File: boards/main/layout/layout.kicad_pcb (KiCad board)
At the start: 4 copper layers, 200 x 100 mm, 115 parts, among them J1 PPPC201LFBN-RC, J10 61300811121, J11 61300811121, J12 SJ1-3523N, J13 61300311121, J14 61300311121, J15 61300811121, J16 61300811121, J17 61300811121, J18 61300811121, J19 USB4085-GF-A, J2 PPPC201LFBN-RC, J3 61301021121, J4 connector, J5 61300211121, J6 61300211121, J7 SJ1-3523N, J8 61300811121, J9 61300811121, U1 ES8388, U10 NE5532DR, U2 ES8388, U3 LP2985-33DBVR, U4 MCP73831-2-OTI/OT, U5 HT8988A, U6 AP2114H-3.3TRG1, U7 CD4052BM96, U8 CD4052BM96, U9 NE5532DR

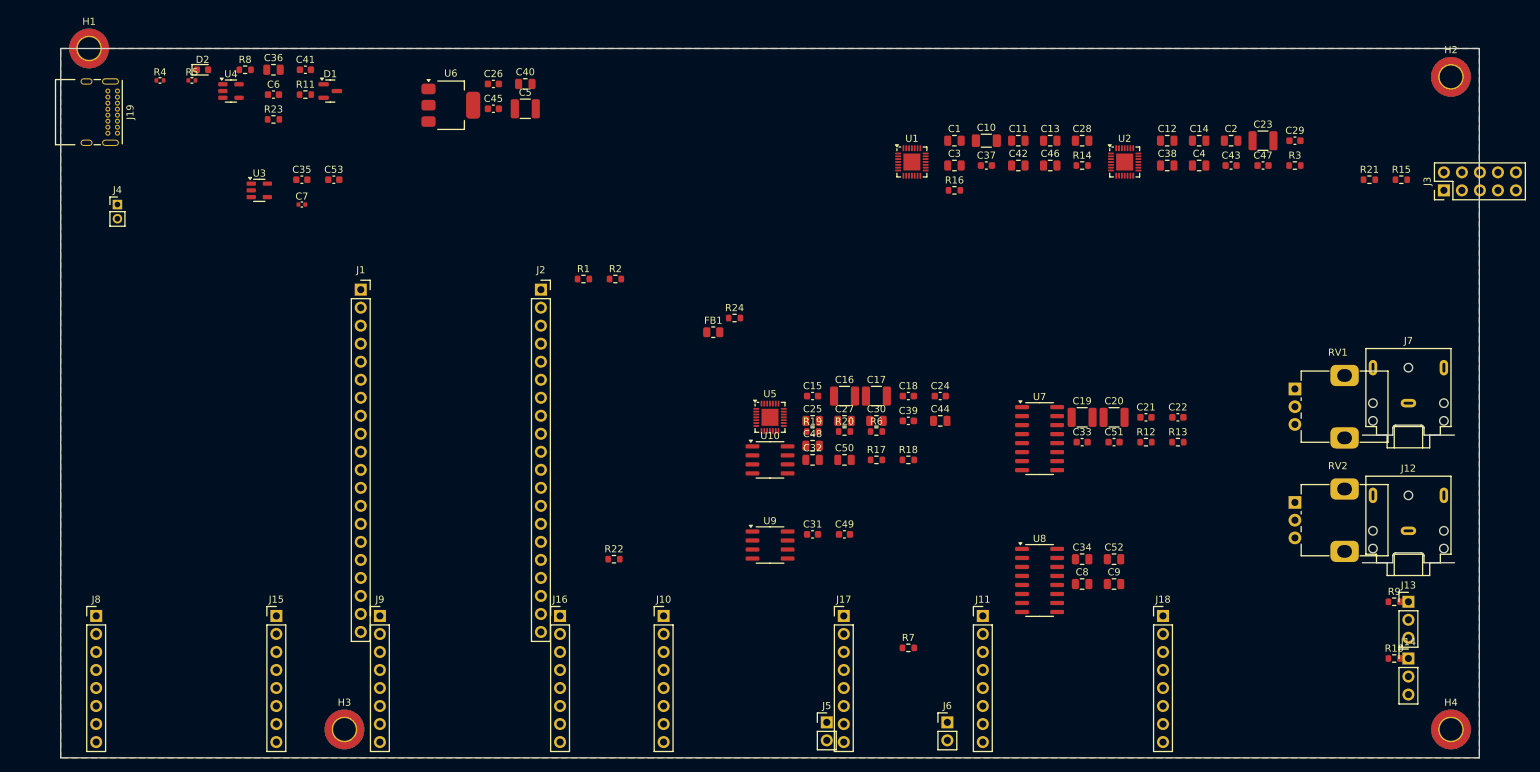
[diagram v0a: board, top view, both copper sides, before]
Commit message: layout changes, main boards smaller
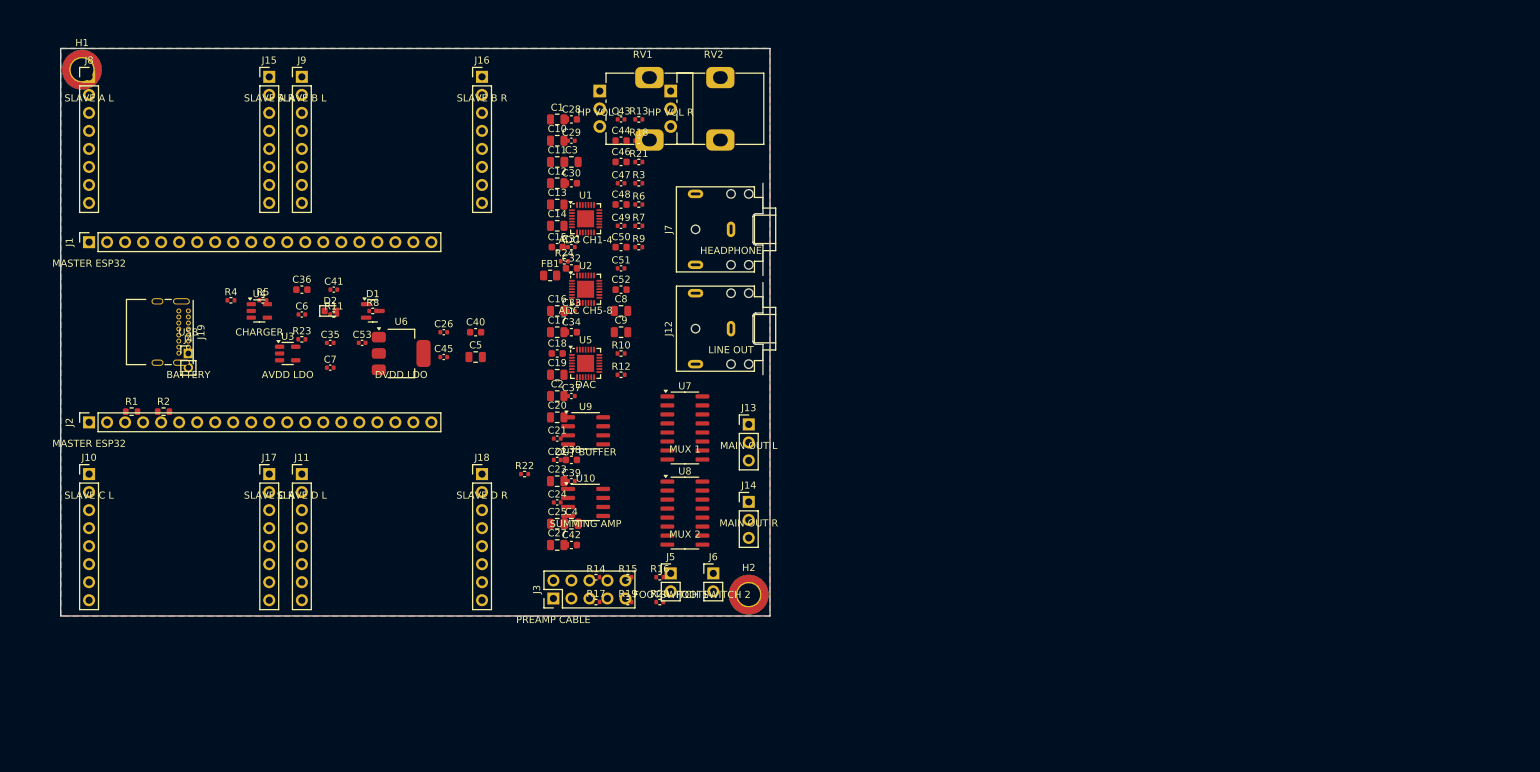
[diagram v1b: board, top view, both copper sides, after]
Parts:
- removed H3, H4: ?, MountingHole_3.2mm_M3_DIN965_Pad_TopBottom
- C10: value GRM31CZ71C226ME15K -> GRM21BZ71A226ME15K; footprint C_1206_3216Metric -> C_0805_2012Metric
- C16, C17, C19, C20, C23, C5: footprint C_1210_3225Metric -> C_0805_2012Metric
- C21, C22, C24, C26, C29, C31, C33, C35, C37, C39, C41, C43, C45, C47, C49, C51, C53, C6: value GRM188R72A104KA35D -> GCM155R71H104KE02D; footprint C_0603_1608Metric -> C_0402_1005Metric
- C28, C30, C32, C34, C36, C38, C40, C42, C44, C46, C48, C50, C52: value GRM21BZ71E106KE15K -> GRM188Z71A106KA73D; footprint C_0805_2012Metric -> C_0603_1608Metric
- R10, R12, R13, R8, R9: value ERJ-3EKF1001V -> ERJ-2RKF1001X; footprint R_0603_1608Metric -> R_0402_1005Metric
- R11: value ERJ-3EKF4701V -> ERJ-2RKF4701X; footprint R_0603_1608Metric -> R_0402_1005Metric
- R14, R15, R16, R17, R18, R19, R20, R21, R22, R3: value ERJ-3EKF1002V -> ERJ-2RKF1002X; footprint R_0603_1608Metric -> R_0402_1005Metric
- R23, R24: value ERJ-3EKF1003V -> ERJ-2RKF1003X; footprint R_0603_1608Metric -> R_0402_1005Metric
- R6, R7: value ERJ-3EKF1201V -> ERJ-2RKF1201X; footprint R_0603_1608Metric -> R_0402_1005Metric
- moved J3 138.1 mm to (79.5, 87.5)
- moved H2 123.0 mm to (107.0, 87.0)
- moved R15 122.6 mm to (90.0, 84.5)
- moved R9 117.7 mm to (91.5, 38.0)
- moved R10 117.2 mm to (89.0, 53.0)
- moved C23 110.5 mm to (80.0, 71.0)
- moved RV1 106.6 mm to (86.0, 16.0)
- moved RV2 105.4 mm to (96.0, 16.0)
- moved R21 103.0 mm to (91.5, 26.0)
- moved C29 102.0 mm to (82.0, 23.0)
- moved C4 101.9 mm to (82.0, 77.0)
- moved C2 101.6 mm to (80.0, 59.0)
- moved J12 99.7 mm to (104.5, 49.5), turned to 90 degrees
- moved J7 98.6 mm to (104.5, 35.5), turned to 90 degrees
- moved J11 98.1 mm to (44.0, 70.0)
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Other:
- board size 200 x 100 mm -> 100 x 80 mm
- board text added: "ADC CH1-4"
- board text added: "ADC CH5-8"
- board text added: "AVDD LDO"
- board text added: "BATTERY"
- board text added: "CHARGER"
- board text added: "DAC"
- board text added: "DVDD LDO"
- board text added: "FOOTSWITCH 1"
- board text added: "FOOTSWITCH 2"
- board text added: "HEADPHONE"
- board text added: "HP VOL L"
- board text added: "HP VOL R"
- board text added: "LINE OUT"
- board text added: "MAIN OUT L"
- board text added: "MAIN OUT R"
- board text added: "MASTER ESP32"
- board text added: "MUX 1"
- board text added: "MUX 2"
- board text added: "OUT BUFFER"
- board text added: "PREAMP CABLE"
- board text added: "SLAVE A L"
- board text added: "SLAVE A R"
- board text added: "SLAVE B L"
- board text added: "SLAVE B R"
- board text added: "SLAVE C L"
- board text added: "SLAVE C R"
- board text added: "SLAVE D L"
- board text added: "SLAVE D R"
- board text added: "SUMMING AMP"
- board text added: "USB"

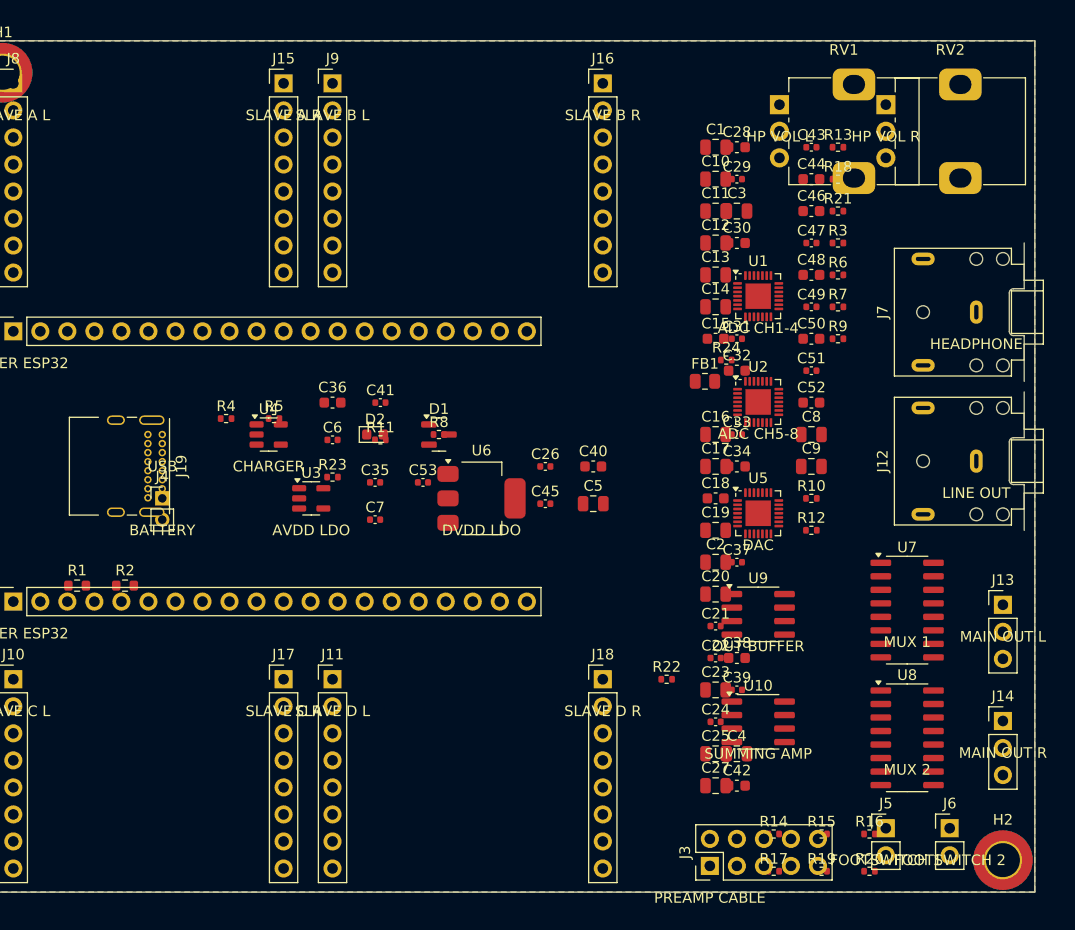
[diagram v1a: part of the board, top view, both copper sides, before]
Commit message: layout improvement
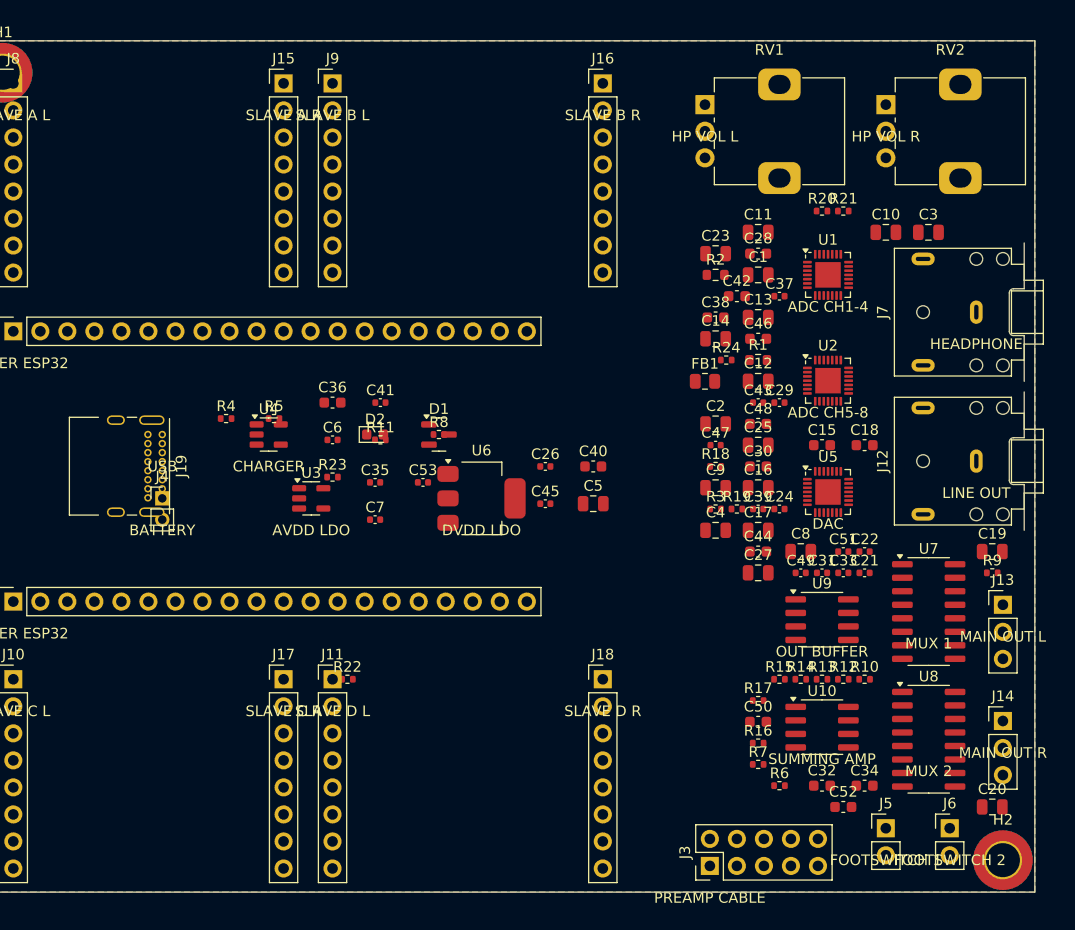
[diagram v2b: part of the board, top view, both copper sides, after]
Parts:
- moved R1 67.4 mm to (84.0, 40.0)
- moved R2 62.7 mm to (80.0, 32.0)
- moved R20 62.2 mm to (90.0, 26.0)
- moved R13 50.0 mm to (90.0, 70.0)
- moved R6 48.3 mm to (86.0, 80.0)
- moved C42 46.0 mm to (82.0, 34.0)
- moved R7 43.6 mm to (84.0, 78.0)
- moved C23 41.0 mm to (80.0, 30.0)
- moved C32 39.8 mm to (90.0, 80.0)
- moved C52 38.1 mm to (92.0, 82.0)
- moved C50 36.3 mm to (84.0, 74.0)
- moved C44 35.4 mm to (84.0, 58.0)
- moved R19 35.0 mm to (82.0, 54.0)
- moved C20 32.8 mm to (106.0, 82.0)
- moved C34 32.3 mm to (94.0, 80.0)
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
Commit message: layout tweaks
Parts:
- moved R21 62.4 mm to (99.0, 88.0)
- moved R20 62.2 mm to (94.5, 88.0)
- moved R22 56.0 mm to (45.4, 14.0)
- moved R18 38.4 mm to (85.5, 88.0)
- moved R19 35.0 mm to (90.0, 88.0)
- moved R17 19.5 mm to (99.0, 84.5)
- moved C8 18.0 mm to (106.0, 58.0)
- moved R2 17.1 mm to (86.0, 48.0)
- moved C38 15.6 mm to (90.0, 48.0)
- moved R15 15.1 mm to (90.0, 84.5)
- moved R14 14.8 mm to (85.5, 84.5)
- moved R16 13.5 mm to (94.5, 84.5)
- moved C18 12.8 mm to (84.0, 56.0)
- moved R1 12.8 mm to (94.0, 48.0)
- moved R13 12.6 mm to (86.0, 58.0)
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
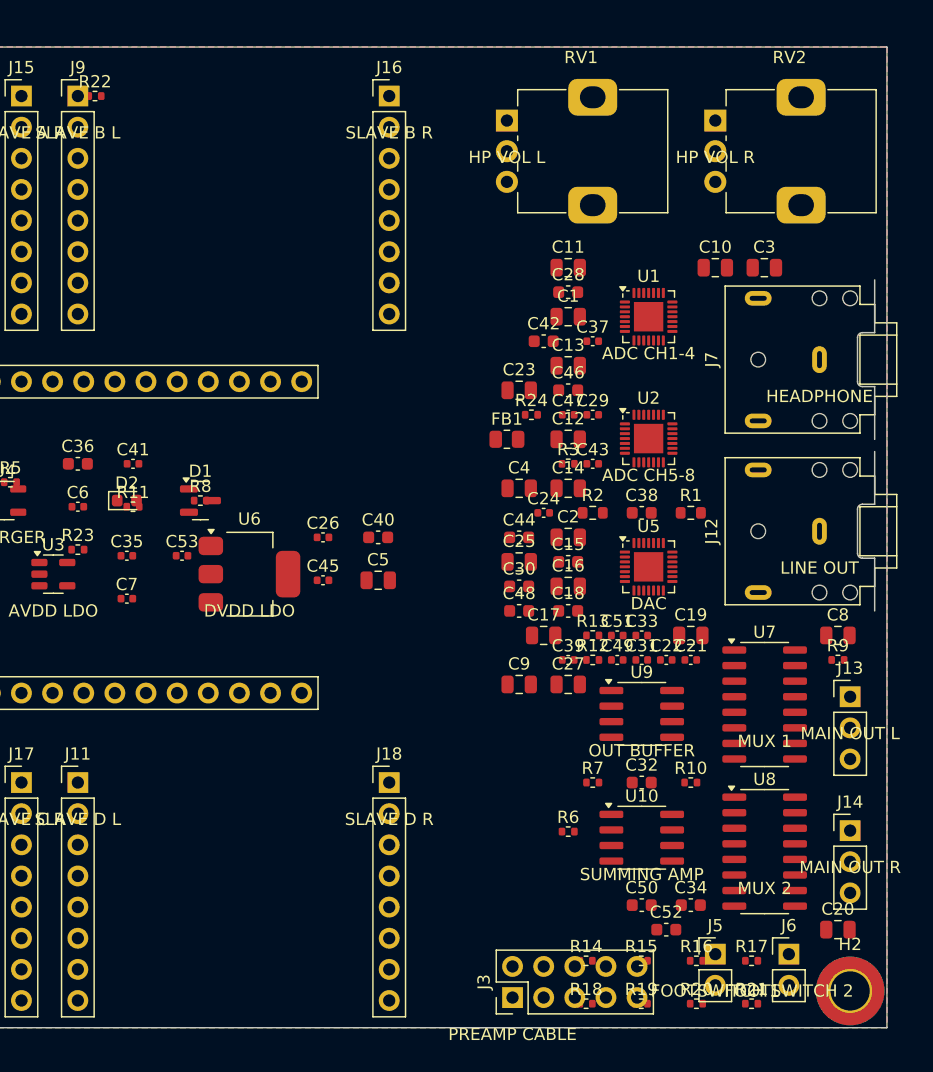
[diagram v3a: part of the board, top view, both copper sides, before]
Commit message: layout fixes
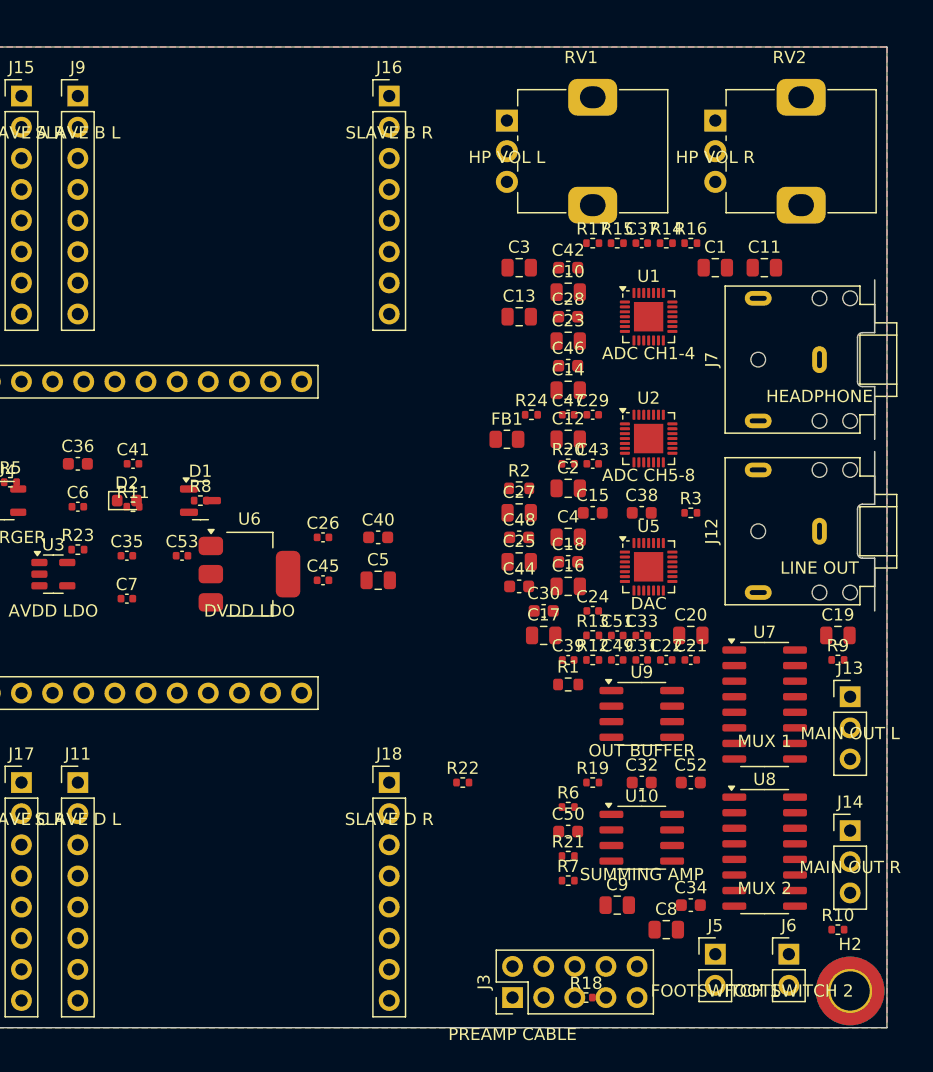
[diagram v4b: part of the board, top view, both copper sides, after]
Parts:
- moved R22 63.5 mm to (75.4, 70.0)
- moved R17 60.0 mm to (86.0, 26.0)
- moved R14 58.9 mm to (92.0, 26.0)
- moved R15 58.6 mm to (88.0, 26.0)
- moved R16 58.5 mm to (94.0, 26.0)
- moved R20 45.3 mm to (84.0, 44.0)
- moved C8 27.8 mm to (92.0, 82.0)
- moved C20 26.8 mm to (94.0, 58.0)
- moved C3 20.0 mm to (80.0, 28.0)
- moved C9 19.7 mm to (88.0, 80.0)
- moved R21 19.2 mm to (84.0, 76.0)
- moved R19 18.5 mm to (86.0, 70.0)
- moved R1 17.2 mm to (84.0, 62.0)
- moved R10 17.0 mm to (106.0, 82.0)
- moved C11 16.0 mm to (100.0, 28.0)
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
